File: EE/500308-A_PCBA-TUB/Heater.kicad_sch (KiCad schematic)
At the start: 5 parts, among them Q1 DMN2075U

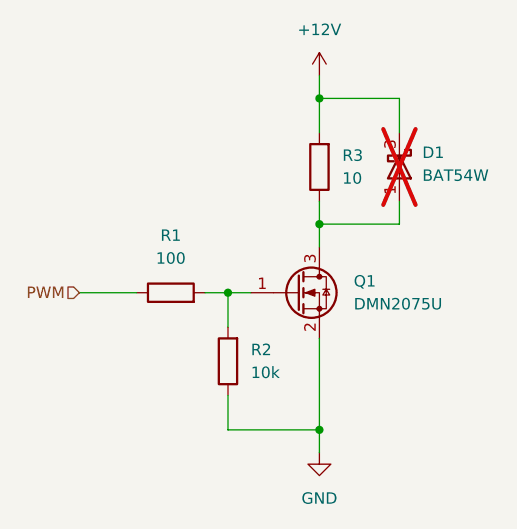
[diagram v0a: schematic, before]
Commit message: Only tmp sensors on well side
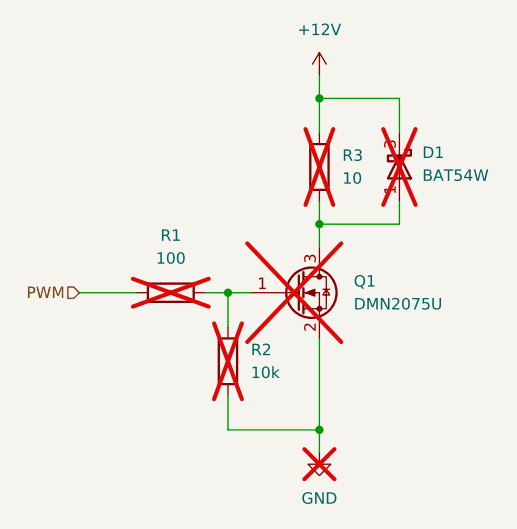
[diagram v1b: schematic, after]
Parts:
- Q1, R1, R2, R3: now not fitted
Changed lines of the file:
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@@
 		(in_bom yes)
 		(on_board yes)
-		(dnp no)
+		(dnp yes)
 		(fields_autoplaced yes)
 		(property "Reference" "R3"
@@
 		(in_bom yes)
 		(on_board yes)
-		(dnp no)
+		(dnp yes)
 		(fields_autoplaced yes)
 		(property "Reference" "R2"
@@
 		(in_bom yes)
 		(on_board yes)
-		(dnp no)
+		(dnp yes)
 		(fields_autoplaced yes)
 		(property "Reference" "R1"
@@
 		(in_bom yes)
 		(on_board yes)
-		(dnp no)
+		(dnp yes)
 		(fields_autoplaced yes)
 		(property "Reference" "Q1"
@@
 		(in_bom yes)
 		(on_board yes)
-		(dnp no)
+		(dnp yes)
 		(fields_autoplaced yes)
 		(property "Reference" "#PWR044"
